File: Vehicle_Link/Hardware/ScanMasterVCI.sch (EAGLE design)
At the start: 89 parts, among them IC1 XMEGA32A4U, IC2 TL331, P1 HARFLEX-1515012-601, Q1 RUM002N05, Q10 ZXMP6A17G, Q3 RUM002N05, Q4 RUM002N05, Q5 RRF015P03, Q6 RUM002N05, Q7 RRF015P03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

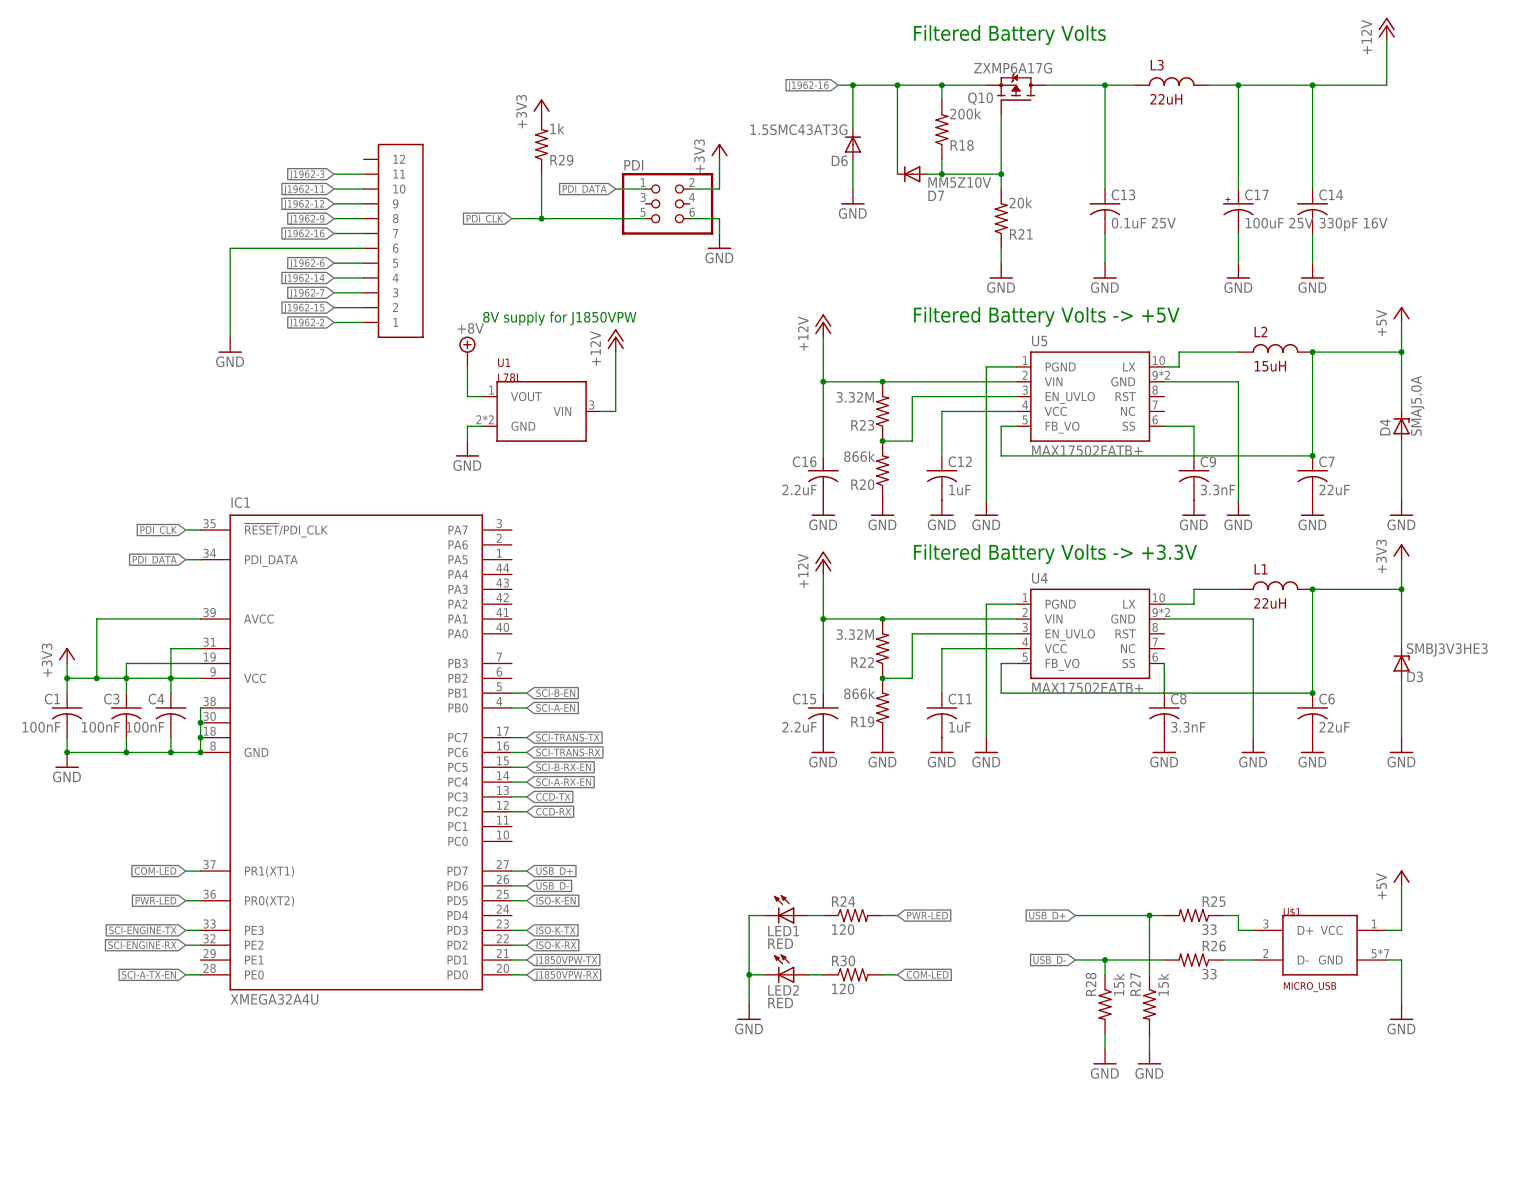
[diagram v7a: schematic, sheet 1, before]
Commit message: Finally swapped out the USB connector for a Bluetooth module, BT823A. Finished the board layout with minimal changes to the comm circuits. Bumped the rev number to D
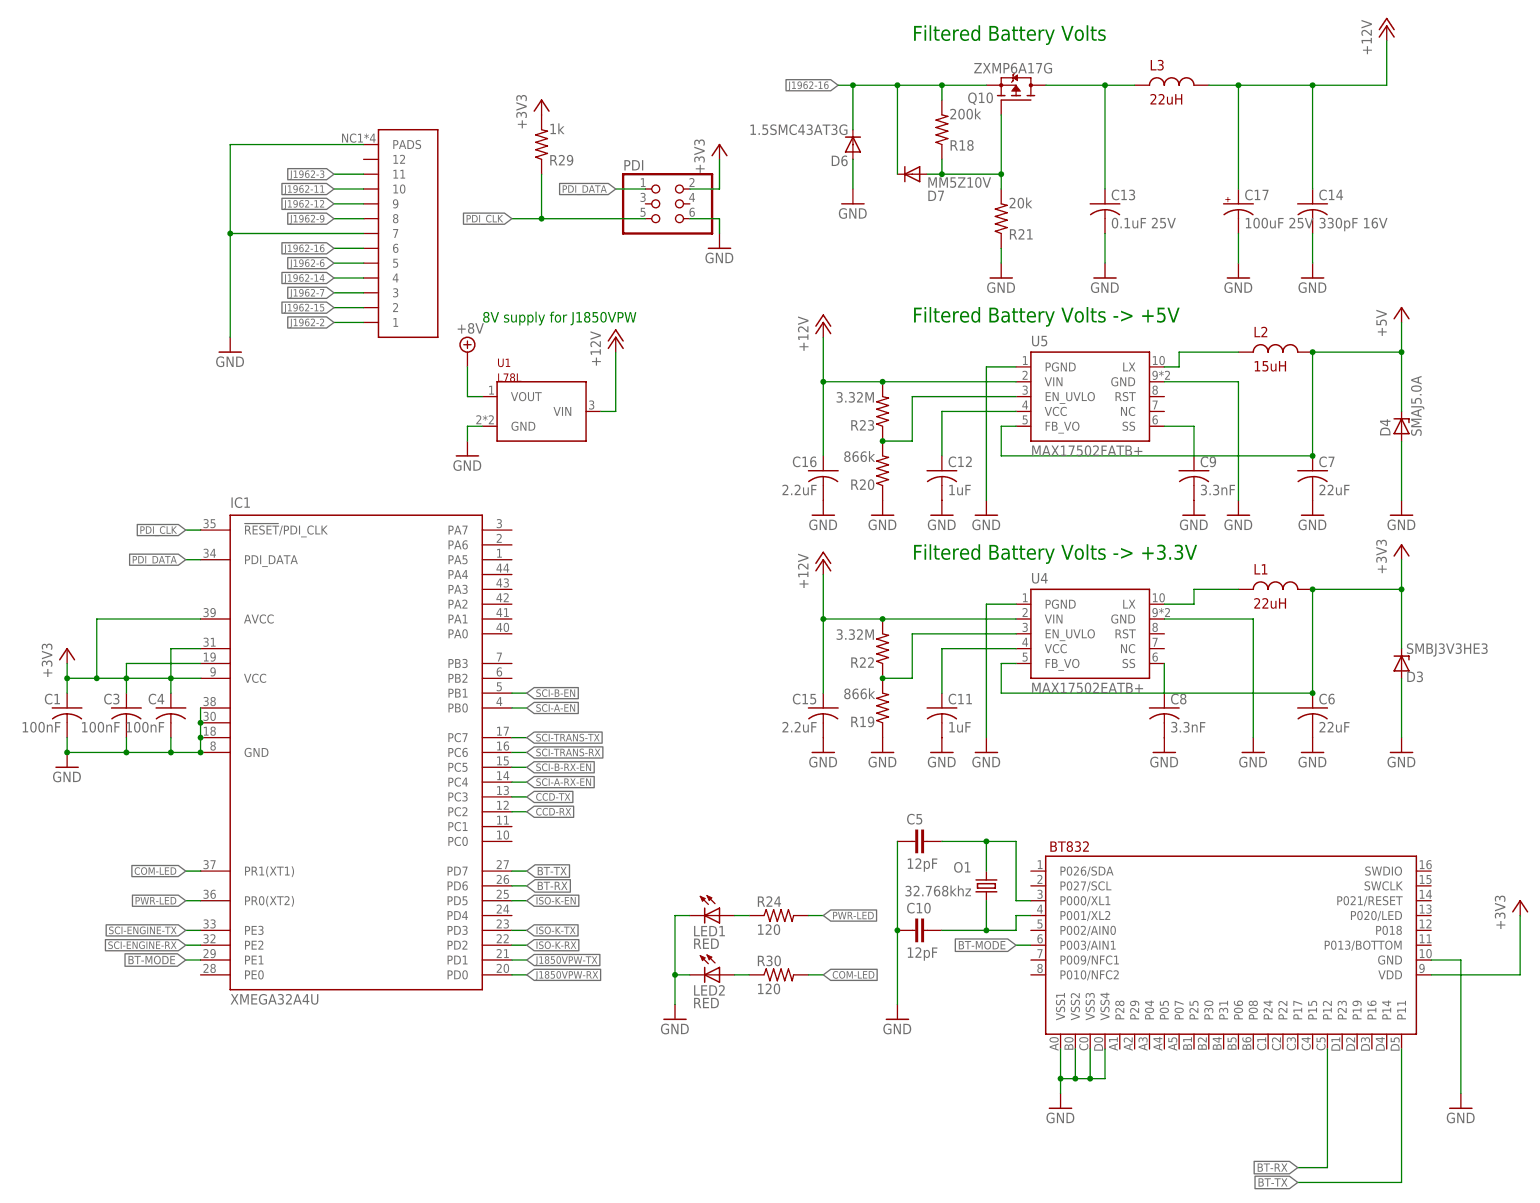
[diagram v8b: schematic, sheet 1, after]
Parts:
- removed R25, R26: 33, adafruit:R-US_R0603
- removed R27, R28: 15k, adafruit:R-US_R0603
- removed R4, R7: 1k, adafruit:R-US_R0603
- removed U$1: MICRO_USB, customics:MICRO_USB
- added C10, C5: 12pF, SparkFun-Capacitors:12PF-0603-50V-5%
- added O1: 32.768khz, customics:SER4103
- added U6: BT832A, customics:BT832A
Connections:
- removed net N$14: R36.1, R41.2, U3B.-IN
- removed net N$25: R26.1, U$1.D-
- removed net SCI-A-TX-EN: IC1.PE0, RN3.4
- removed net USB_D+: IC1.PD7, R25.2, R27.1
- removed net USB_D-: IC1.PD6, R26.2, R28.1
- new net BT-MODE: IC1.PE1, U6.P003/AIN1
- new net BT-RX: IC1.PD6, U6.P12
- new net BT-TX: IC1.PD7, U6.P11
- new net N$13: C5.2, O1.2, U6.P000/XL1
- net +3V3: now also U6.VDD
- net +5V: no longer R4.2, U$1.VCC
- net CCD-RX: now also RN3.2; no longer RN3.1
- net CCD-TX: now also RN3.1; no longer RN3.2
- net GND: now also C10.1, C5.1, P1.7, P1.PADS, U6.GND, U6.VSS1, U6.VSS2, U6.VSS3, U6.VSS4; no longer P1.6, R27.2, R28.2, R7.1, U$1.GND
- net J1962-16: now also P1.6; no longer P1.7
- net N$24: now also C10.2, O1.1, U6.P001/XL2; no longer R25.1, U$1.D+
- net N$6: now also R36.1, R41.2, U3B.-IN; no longer R4.1, R7.2
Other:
- moved on the sheet: LED1, LED2, R24, R30, U3D
